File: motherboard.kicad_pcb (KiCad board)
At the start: 2 copper layers, 100 x 100 mm, 140 parts, among them J1 USB_C_Receptacle_USB2.0, J10 Power input, J11 Bed, J12 Hotend, J13 X_LIMIT, J14 Y_LIMIT, J15 Z_LIMIT, J2 I2C, J3 EXP1, J4 EXP2, J5 BFP_touch, J6 FAN1, J8 BED_TEMP, J9 HOTEND_TEMP, M1 NEMA17, M2 NEMA17, M3 NEMA17, M4 NEMA17, Q1 BC847, Q2 BC847, Q3 AO3400A, Q5 APM4010, Q6 APM4010, U1 MP1584, U2 STM32F103C8Tx, U3 CH340G, U4 A4988, U5 A4988, U6 A4988, U7 A4988, Y1 8MHz, Y2 12MHz

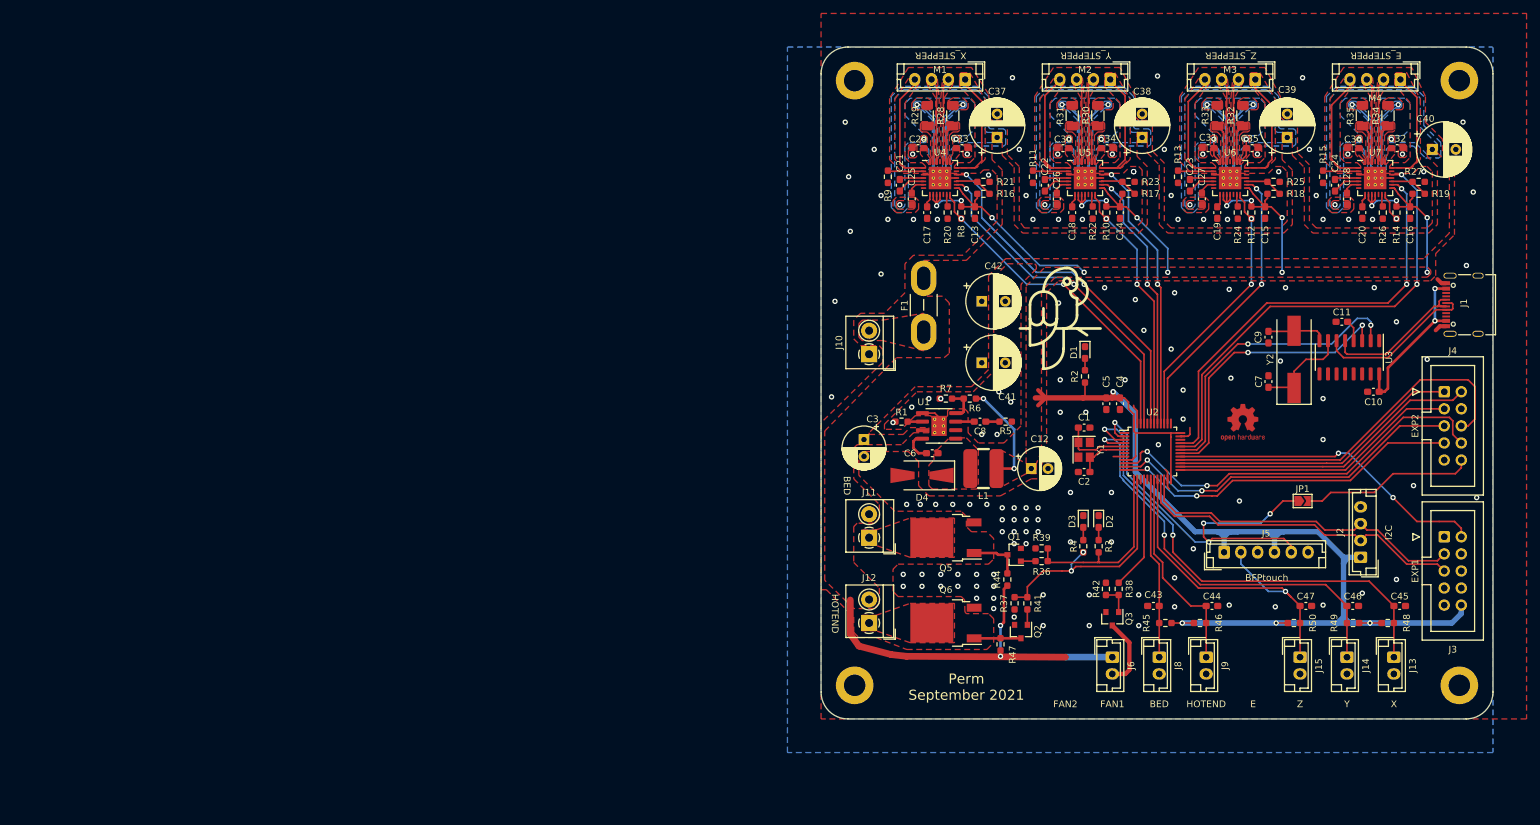
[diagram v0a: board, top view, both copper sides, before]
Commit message: new pcb and fix schematic
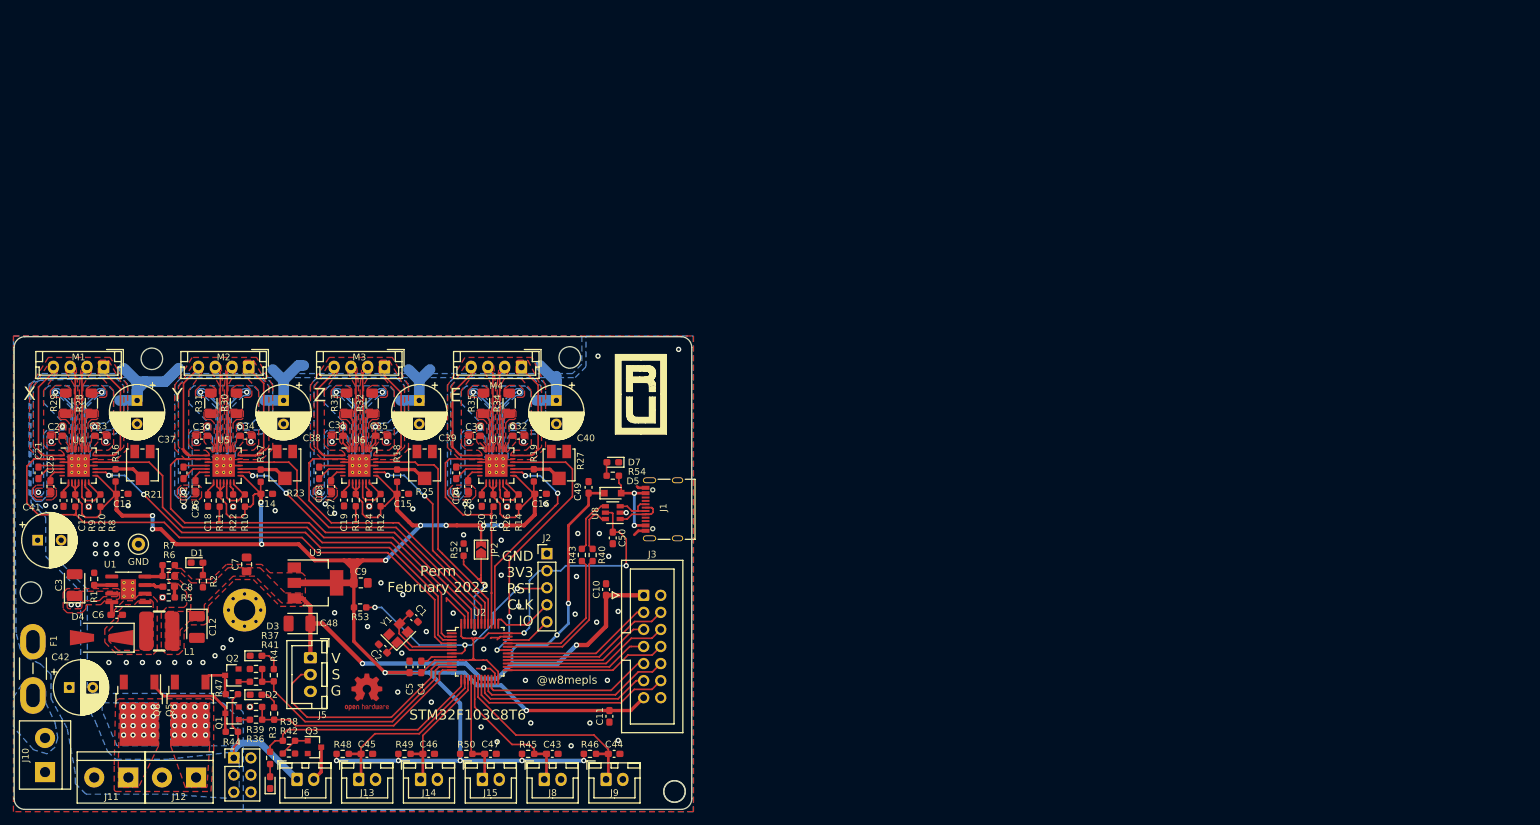
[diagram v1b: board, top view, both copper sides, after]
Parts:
- removed  : Parrot_2, Footprints:Parrot_2
- removed J4: EXP2, Connector_IDC:IDC-Header_2x05_P2.54mm_Vertical
- removed JP1: Jumper, Jumper:SolderJumper-2_P1.3mm_Open_TrianglePad1.0x1.5mm
- removed the REF** at (245.0, 145.0)
- removed the REF** at (155.0, 145.0)
- removed the REF** at (155.0, 55.0)
- removed the REF** at (245.0, 55.0)
- removed Y2: 12MHz, Crystal:Crystal_SMD_HC49-SD
- added C48: 10u, Capacitor_Tantalum_SMD:CP_EIA-3528-21_Kemet-B_Pad1.50x2.35mm_HandSolder, F.Cu at (72.4, 135.8)
- added C49: 0u1, Capacitor_SMD:C_0603_1608Metric_Pad1.08x0.95mm_HandSolder, F.Cu at (115.4, 115.5)
- added C50: 0u1, Capacitor_SMD:C_0603_1608Metric_Pad1.08x0.95mm_HandSolder, F.Cu at (119.0, 123.1)
- added D5: D_Schottky, Diode_SMD:D_SOD-323_HandSoldering, F.Cu at (119.0, 116.4)
- added D6: LED, LED_SMD:LED_0603_1608Metric_Pad1.05x0.95mm_HandSolder, F.Cu at (68.0, 159.5)
- added D7: LED, LED_SMD:LED_0603_1608Metric_Pad1.05x0.95mm_HandSolder, F.Cu at (119.0, 111.8)
- added GND: TestPoint_Loop_D1.80mm_Drill1.0mm_Beaded, TestPoint:TestPoint_Loop_D1.80mm_Drill1.0mm_Beaded, F.Cu at (48.4, 124.0)
- added J7: Conn_02x03_Odd_Even, Connector_PinHeader_2.54mm:PinHeader_2x03_P2.54mm_Vertical, F.Cu at (62.6, 155.8)
- added JP2: BOOT, Jumper:SolderJumper-2_P1.3mm_Open_TrianglePad1.0x1.5mm, F.Cu at (99.4, 124.8)
- added R40: 22, Resistor_SMD:R_0603_1608Metric_Pad0.98x0.95mm_HandSolder, F.Cu at (116.0, 125.6)
- added R43: 22, Resistor_SMD:R_0603_1608Metric_Pad0.98x0.95mm_HandSolder, F.Cu at (114.4, 125.6)
- added R51: 1k, Resistor_SMD:R_0603_1608Metric_Pad0.98x0.95mm_HandSolder, F.Cu at (68.0, 155.8)
- added R52: 10k, Resistor_SMD:R_0603_1608Metric_Pad0.98x0.95mm_HandSolder, F.Cu at (96.8, 124.8)
- added R53: 10k, Resistor_SMD:R_0603_1608Metric_Pad0.98x0.95mm_HandSolder, F.Cu at (81.4, 133.4)
- added R54: 1k, Resistor_SMD:R_0603_1608Metric_Pad0.98x0.95mm_HandSolder, F.Cu at (119.0, 113.8)
- added REF**: Made_in_Russia, Footprints:Made_in_Russia, F.Cu at (119.4, 107.6)
- added REF**: MountingHole_3.2mm_M3_Pad_Via, MountingHole:MountingHole_3.2mm_M3_Pad_Via, F.Cu at (64.2, 133.8)
- added REF**: MountingHole_3.2mm_M3_ISO14580, MountingHole:MountingHole_3.2mm_M3_ISO14580, F.Cu at (112.6, 96.2)
- added REF**: MountingHole_3.2mm_M3_ISO14580, MountingHole:MountingHole_3.2mm_M3_ISO14580, F.Cu at (50.4, 96.4)
- added REF**: MountingHole_3.2mm_M3_ISO14580, MountingHole:MountingHole_3.2mm_M3_ISO14580, F.Cu at (32.4, 131.2)
- added REF**: MountingHole_3.2mm_M3_ISO14580, MountingHole:MountingHole_3.2mm_M3_ISO14580, F.Cu at (128.2, 160.8)
- added U8: USBLC6-2SC6, Package_TO_SOT_SMD:SOT-23-6, F.Cu at (119.0, 119.3)
- C10: value 1u -> 0u1
- C11: value 10n -> 0u1
- C12, C3: footprint Capacitor_THT:CP_Radial_D6.3mm_P2.50mm -> Capacitor_Tantalum_SMD:CP_EIA-3528-21_Kemet-B_Pad1.50x2.35mm_HandSolder
- C7, C9: value 22p -> 10u; footprint Capacitor_SMD:C_0603_1608Metric_Pad1.08x0.95mm_HandSolder -> Capacitor_SMD:C_0805_2012Metric_Pad1.18x1.45mm_HandSolder
- J10, J11, J12: footprint TerminalBlock_4Ucon:TerminalBlock_4Ucon_1x02_P3.50mm_Horizontal -> TerminalBlock:TerminalBlock_bornier-2_P5.08mm
- J13, J14, J15, J8, J9: footprint Connector_JST:JST_EH_B2B-EH-A_1x02_P2.50mm_Vertical -> Connector_JST:JST_XH_B2B-XH-A_1x02_P2.50mm_Vertical
- J2: value I2C -> SWD; footprint Connector_JST:JST_EH_B4B-EH-A_1x04_P2.50mm_Vertical -> Connector_PinHeader_2.54mm:PinHeader_1x05_P2.54mm_Vertical
- J3: value EXP1 -> EXP; footprint Connector_IDC:IDC-Header_2x05_P2.54mm_Vertical -> Connector_IDC:IDC-Header_2x07_P2.54mm_Vertical
- J5: value BFP_touch -> Conn_01x03; footprint Connector_JST:JST_EH_B6B-EH-A_1x06_P2.50mm_Vertical -> Connector_JST:JST_XH_B3B-XH-A_1x03_P2.50mm_Vertical
- J6: value FAN1 -> FAN; footprint Connector_JST:JST_EH_B2B-EH-A_1x02_P2.50mm_Vertical -> Connector_JST:JST_XH_B2B-XH-A_1x02_P2.50mm_Vertical
- R21, R23, R25, R27: footprint Resistor_SMD:R_0603_1608Metric_Pad0.98x0.95mm_HandSolder -> Potentiometer_SMD:Potentiometer_Bourns_3314J_Vertical
- U3: value CH340G -> AMS1117-3.3; footprint Package_SO:SOIC-16_3.9x9.9mm_P1.27mm -> Package_TO_SOT_SMD:SOT-223-3_TabPin2
- moved U3 157.5 mm to (74.8, 129.8), turned to 0 degrees
- moved R48 156.8 mm to (78.8, 155.2)
- moved C45 155.3 mm to (82.4, 155.2)
- moved J13 155.1 mm to (81.2, 159.0), turned to 0 degrees
- moved C7 154.5 mm to (64.5, 127.0)
- moved C42 147.5 mm to (38.1, 145.3)
- moved F1 143.2 mm to (32.7, 146.5)
- moved C41 143.0 mm to (33.4, 123.4)
- moved R49 142.5 mm to (88.0, 155.2), turned to 0 degrees
- moved C9 139.9 mm to (81.5, 129.8), turned to 0 degrees
- moved C46 139.3 mm to (91.6, 155.2)
- moved J14 139.1 mm to (90.4, 159.0), turned to 0 degrees
- moved R19 138.2 mm to (107.2, 113.8), turned to 270 degrees
- moved C20 137.9 mm to (99.5, 117.5)
- moved C24 137.6 mm to (95.7, 113.4)
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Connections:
- C10 pad 1: GND -> +5V
- C10 pad 2: Net-(C10-Pad2) -> GND
- C11 pad 2: Net-(C11-Pad2) -> +3V3
- C12 pad 1: +3V3 -> +5V
- C7 pad 1: Net-(C7-Pad1) -> +5V
- C9 pad 1: Net-(C9-Pad1) -> +3V3
- J1 pad A4: Net-(C10-Pad2) -> /PC_CONN
- J1 pad A9: Net-(C10-Pad2) -> /PC_CONN
- J1 pad B4: Net-(C10-Pad2) -> /PC_CONN
- J1 pad B9: Net-(C10-Pad2) -> /PC_CONN
- J2 pad 1: +3V3 -> GND
- J2 pad 2: /SCL -> +3V3
- J2 pad 3: /SDA -> /NRST
- J2 pad 4: GND -> /PA14
- J3 pad 1: /BEEPER -> +5V
- J3 pad 10: +3V3 -> /SCL
- J3 pad 2: /ENC_PUSH -> GND
- J3 pad 3: /SDA -> /CARD-DETECT
- J3 pad 4: Net-(J3-Pad4) -> /SPI_RESET
- J3 pad 5: /SCL -> /SPI_MOSI
- J3 pad 6: Net-(J3-Pad6) -> /SPI_MISO
- J3 pad 7: Net-(J3-Pad7) -> /SPI_SCK
- J3 pad 8: Net-(J3-Pad8) -> /ENC_PUSH
- J3 pad 9: GND -> /SDA
- J5 pad 1: +3V3 -> +5V
- J5 pad 2: /Z_STOP -> /SERVO
- L1 pad 2: +3V3 -> +5V
- R10 pad 2: /Y_SLEEP -> Net-(R10-Pad2)
- R11 pad 1: GND -> +3V3
- R11 pad 2: Net-(R11-Pad2) -> /Y_SLEEP
- R12 pad 2: /Z_SLEEP -> Net-(R12-Pad2)
- R13 pad 1: GND -> +3V3
- R13 pad 2: Net-(R13-Pad2) -> /Z_SLEEP
- R14 pad 2: /E_SLEEP -> Net-(R14-Pad2)
- R15 pad 1: GND -> +3V3
- R15 pad 2: Net-(R15-Pad2) -> /E_SLEEP
- R2 pad 1: +3V3 -> +5V
- R38 pad 2: /FAN1_MOSFET -> /FAN_MOSFET
- R6 pad 1: +3V3 -> +5V
- R8 pad 2: /X_SLEEP -> Net-(R8-Pad2)
- R9 pad 1: GND -> +3V3
- R9 pad 2: Net-(R9-Pad2) -> /X_SLEEP
- U2 pad 10: /SPI_RESET -> /SERVO
- U2 pad 11: /ENC_B -> /HOTEND_MOSFET
- U2 pad 12: /CARD-DETECT -> /BED_MOSFET
- U2 pad 13: /BED_MOSFET -> /FAN_MOSFET
- U2 pad 14: /HOTEND_MOSFET -> /X_STOP
- U2 pad 15: /FAN2_MOSFET -> /Y_STOP
- U2 pad 16: /FAN1_MOSFET -> /Z_STOP
- U2 pad 17: /E_STOP -> /BED_THERM
- U2 pad 18: /BED_THERM -> /HOTEND_THERM
- U2 pad 19: /HOTEND_THERM -> /ENC_B
- U2 pad 2: /SERVO -> /X_DIR
- U2 pad 20: /Z_STOP -> /ENC_A
- U2 pad 25: /ENC_A -> /ENC_PUSH
- U2 pad 29: /ENC_PUSH -> /SPI_RESET
- U2 pad 3: /X_STOP -> /X_STEP
- U2 pad 30: /TX -> /CARD-DETECT
- U2 pad 31: /RX -> /E_DIR
- U2 pad 32: /E_DIR -> /D-
- U2 pad 33: /E_STEP -> /D+
- U2 pad 34: /E_SLEEP -> /PA13
- U2 pad 37: /Z_DIR -> /PA14
- U2 pad 38: /Z_STEP -> /E_STEP
- U2 pad 39: /Z_SLEEP -> /E_SLEEP
- U2 pad 4: /Y_STOP -> /X_SLEEP
- U2 pad 40: /Y_DIR -> /Z_DIR
- U2 pad 41: /Y_STEP -> /Z_STEP
- U2 pad 42: /Y_SLEEP -> /Z_SLEEP
- U2 pad 43: /X_DIR -> /Y_DIR
- U2 pad 45: /X_STEP -> /Y_STEP
- U2 pad 46: /X_SLEEP -> /Y_SLEEP
- U3 pad 2: /RX -> +3V3
- U3 pad 3: /TX -> +5V
- U4 pad 12: Net-(U4-Pad12) -> Net-(R8-Pad2)
- U4 pad 14: /X_SLEEP -> Net-(R8-Pad2)
- U4 pad 2: Net-(R9-Pad2) -> /X_SLEEP
- U5 pad 12: Net-(U5-Pad12) -> Net-(R10-Pad2)
- U5 pad 14: /Y_SLEEP -> Net-(R10-Pad2)
- U5 pad 2: Net-(R11-Pad2) -> /Y_SLEEP
- U6 pad 12: Net-(U6-Pad12) -> Net-(R12-Pad2)
- U6 pad 14: /Z_SLEEP -> Net-(R12-Pad2)
- U6 pad 2: Net-(R13-Pad2) -> /Z_SLEEP
- U7 pad 12: Net-(U7-Pad12) -> Net-(R14-Pad2)
- U7 pad 14: /E_SLEEP -> Net-(R14-Pad2)
- U7 pad 2: Net-(R15-Pad2) -> /E_SLEEP
- Y1 pad 1: Net-(C1-Pad2) -> Net-(C2-Pad1)
- Y1 pad 3: Net-(C2-Pad1) -> Net-(C1-Pad2)
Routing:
- net +5V: track 0.00 -> 106.8 mm, vias 0 -> 4
- net +3V3: track 330.7 -> 383.9 mm, vias 22 -> 18
- net /RX: track 45.1 -> 0.00 mm, vias 2 -> 0
- net /X_STOP: track 71.0 -> 27.1 mm, vias 2 -> 0
- net /TX: track 42.9 -> 0.00 mm, vias 2 -> 0
- net /Y_STOP: track 62.3 -> 19.6 mm, vias 2 -> 0
- net /X_SLEEP: track 49.1 -> 87.9 mm, vias 2 -> 0
- net /Z_STOP: track 53.7 -> 16.9 mm, vias 1 -> 0
- net /NRST: track 0.00 -> 36.6 mm, vias 0 -> 3
- net /Z_DIR: track 0.00 -> 35.8 mm
- net /SPI_RESET: track 60.5 -> 25.5 mm, vias 2 -> 0
- net /FAN_MOSFET: track 0.00 -> 34.5 mm
- net /SPI_MOSI: track 56.5 -> 22.1 mm
- net /E_STEP: track 65.5 -> 31.3 mm
- net /E_SLEEP: track 4.30 -> 36.4 mm, vias 1 -> 0
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- added copper zone on F.Cu, net +5V
- added copper zone on B.Cu, net Net-(F1-Pad1)
- added copper zone on B.Cu, net Net-(J11-Pad1)
- added copper zone on B.Cu, net Net-(J12-Pad1)
- removed copper zone on F.Cu, net +3V3
- removed copper zone on F.Cu, net Net-(F1-Pad1)
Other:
- board size 100 x 100 mm -> 100.9 x 70.4 mm
- board text added: "+ -"
- board text added: "1A 1B 2A 2B"
- board text added: "@w8mepls"
- board text added: "FAN"
- board text added: "GND 3V3 RST CLK IO"
- board text added: "INPUT"
- board text added: "ITS TEST BOARD! AN ERROR MAY OCCUR, RESULTING IN A FIRE"
- board text added: "OUTPUT"
- board text added: "Perm February 2022"
- board text added: "STM32F103C8T6"
- board text added: "TH-BED"
- board text added: "TH-HOT"
- board text added: "V S G"
- board text added: "X-STOP"
- board text added: "Y-STOP"
- board text added: "Z-STOP"
- board text added: "{\c16737820;{\W1.000;}}"
- board text removed: "BFPtouch"
- board text removed: "EXP1"
- board text removed: "EXP2"
- board text removed: "E_STEPPER"
- board text removed: "FAN1"
- board text removed: "FAN2"
- board text removed: "I2C"
- board text removed: "Perm September 2021"
- board text removed: "X_STEPPER"
- board text removed: "Y_STEPPER"
- board text removed: "Z_STEPPER"

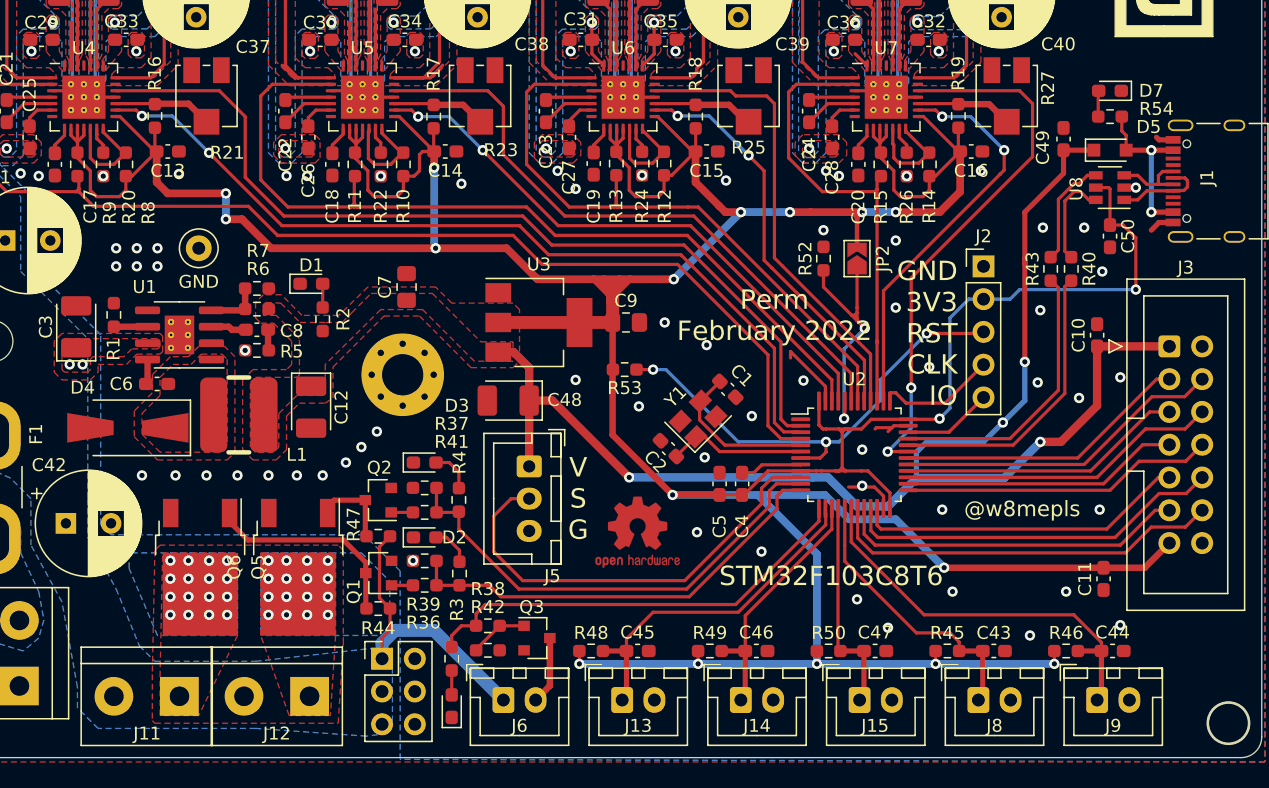
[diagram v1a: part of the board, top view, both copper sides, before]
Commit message: change connection from USB to UART to support STM32 without USB
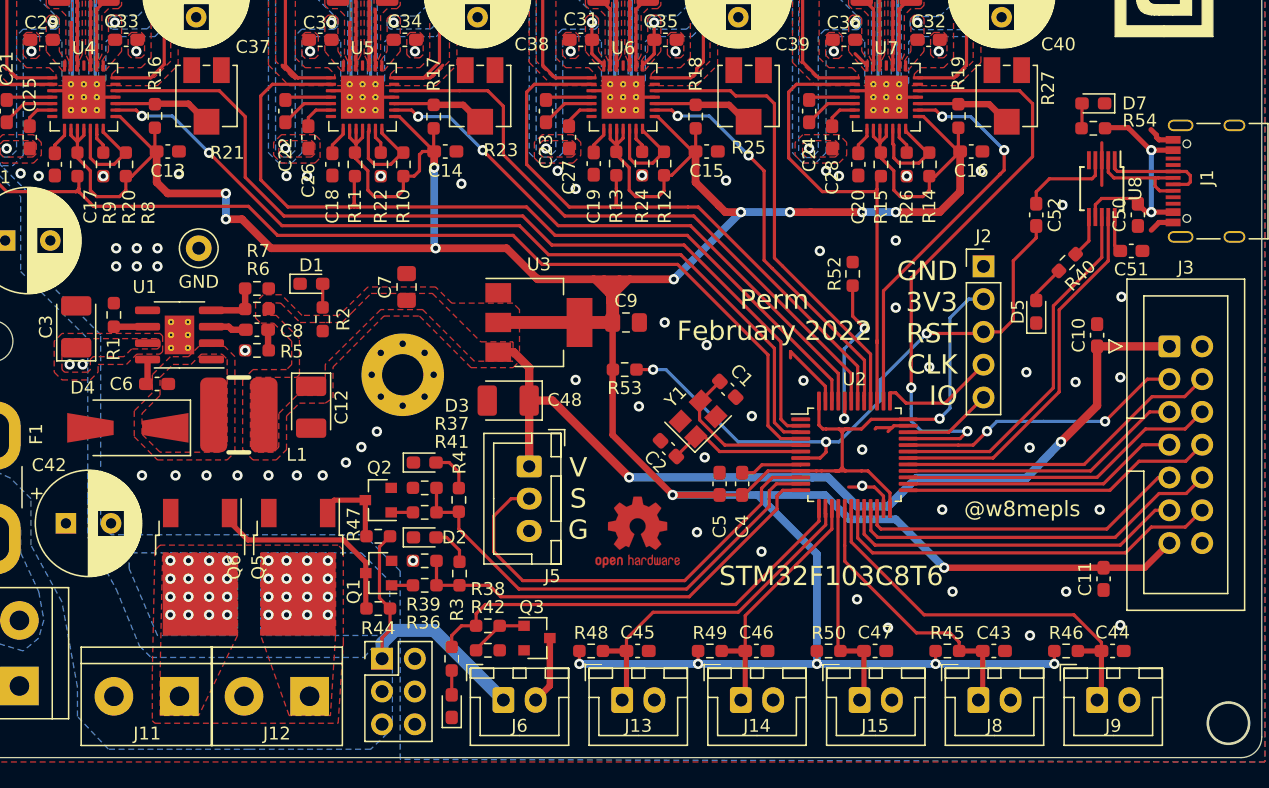
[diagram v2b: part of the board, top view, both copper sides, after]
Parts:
- removed C49: 0u1, Capacitor_SMD:C_0603_1608Metric_Pad1.08x0.95mm_HandSolder
- removed JP2: BOOT, Jumper:SolderJumper-2_P1.3mm_Open_TrianglePad1.0x1.5mm
- removed R43: 22, Resistor_SMD:R_0603_1608Metric_Pad0.98x0.95mm_HandSolder
- added C51: 0u1, Capacitor_SMD:C_0603_1608Metric_Pad1.08x0.95mm_HandSolder, F.Cu at (120.7, 124.2)
- added C52: 0u1, Capacitor_SMD:C_0603_1608Metric_Pad1.08x0.95mm_HandSolder, F.Cu at (113.3, 121.4)
- D5: value D_Schottky -> LED; footprint Diode_SMD:D_SOD-323_HandSoldering -> LED_SMD:LED_0603_1608Metric_Pad1.05x0.95mm_HandSolder
- R40: value 22 -> 1k
- U8: value USBLC6-2SC6 -> CH340E; footprint Package_TO_SOT_SMD:SOT-23-6 -> Package_SO:MSOP-10_3x3mm_P0.5mm
- moved D5 13.8 mm to (113.3, 128.9), turned to 90 degrees
- moved C50 2.72 mm to (121.2, 121.4)
- moved R52 2.55 mm to (99.1, 126.0)
- moved D7 1.62 mm to (117.7, 112.8)
- moved R54 1.58 mm to (117.7, 114.7)
- moved U8 0.64 mm to (118.4, 119.4), turned to 270 degrees
- moved R40 0.59 mm to (115.7, 125.1), turned to 225 degrees
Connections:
- C50 pad 2: +3V3 -> /PC_CONN
- D5 pad 1: +5V -> GND
- D5 pad 2: /PC_CONN -> Net-(D5-Pad2)
- J1 pad A6: Net-(J1-PadA6) -> /D+
- J1 pad A7: Net-(J1-PadA7) -> /D-
- J1 pad B6: Net-(J1-PadA6) -> /D+
- J1 pad B7: Net-(J1-PadA7) -> /D-
- R40 pad 1: /D- -> Net-(R40-Pad1)
- R40 pad 2: Net-(R40-Pad2) -> Net-(D5-Pad2)
- U2 pad 30: /CARD-DETECT -> /RX
- U2 pad 31: /E_DIR -> /TX
- U2 pad 32: /D- -> /CARD-DETECT
- U2 pad 33: /D+ -> /E_DIR
- U8 pad 1: Net-(J1-PadA7) -> /D+
- U8 pad 2: GND -> /D-
- U8 pad 3: Net-(J1-PadA6) -> GND
- U8 pad 5: +3V3 -> Net-(U8-Pad5)
- U8 pad 6: Net-(R40-Pad2) -> Net-(R40-Pad1)
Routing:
- net +5V: track 106.8 -> 71.4 mm, vias 4 -> 2
- net /RX: track 0.00 -> 28.9 mm
- net /TX: track 0.00 -> 28.1 mm
- net +3V3: track 383.9 -> 357.4 mm, vias 18 -> 17
- net /D-: track 22.8 -> 8.32 mm
- net /D+: track 22.0 -> 8.65 mm
- net /NRST: track 36.6 -> 47.3 mm
- net Net-(R40-Pad2): track 7.58 -> 0.00 mm
- net Net-(J1-PadA7): track 7.01 -> 0.00 mm
- net /BOOT0: track 19.7 -> 12.7 mm
- net Net-(J1-PadA6): track 6.05 -> 0.00 mm
- net /PC_CONN: track 12.9 -> 18.4 mm
- net /E_DIR: track 42.5 -> 47.3 mm
- net Net-(R40-Pad1): track 0.00 -> 3.31 mm
- net GND: track 142.6 -> 145.7 mm, vias 83 -> 81
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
